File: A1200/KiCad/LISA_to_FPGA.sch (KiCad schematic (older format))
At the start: 27 parts, among them J1 Conn_01x04, J2 Conn_01x40, U1 LM1117-3.3, U2 74LVC162244ADGG, U3 74LVC162244ADGG, U4 LISA, U5 RP2354B

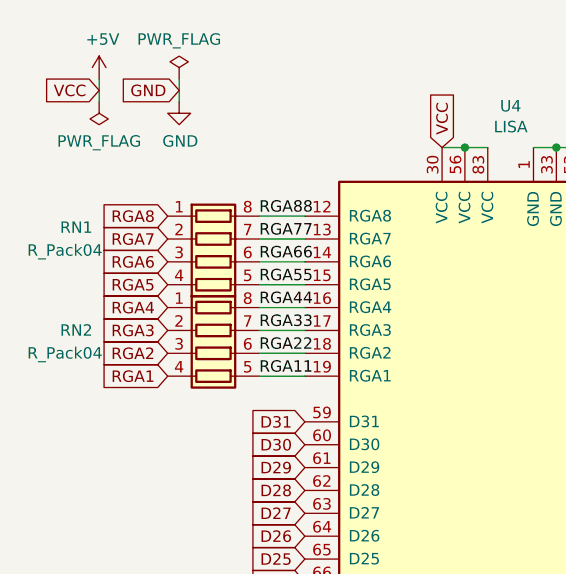
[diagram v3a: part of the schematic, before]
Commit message: Go to 4 layer and route RGA tracks
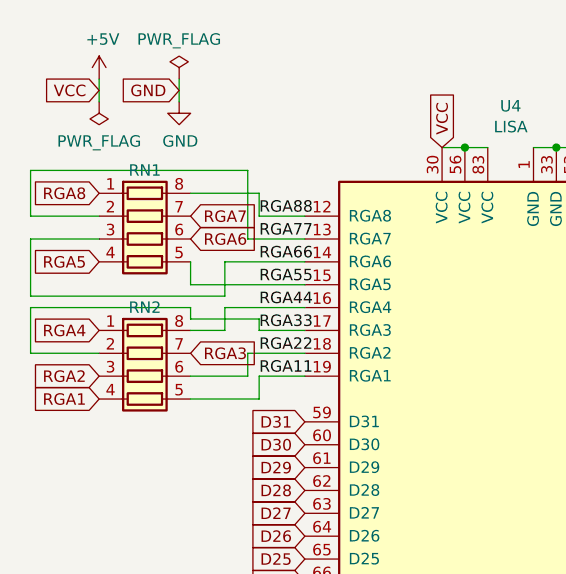
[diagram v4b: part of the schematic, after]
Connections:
- net RGA3: now also RN2.7 (R2.2); no longer RN2.2 (R2.1)
- net RGA33: now also RN2.2 (R2.1); no longer RN2.7 (R2.2)
- net RGA6: now also RN1.6 (R3.2); no longer RN1.3 (R3.1)
- net RGA66: now also RN1.3 (R3.1); no longer RN1.6 (R3.2)
- net RGA7: now also RN1.7 (R2.2); no longer RN1.2 (R2.1)
- net RGA77: now also RN1.2 (R2.1); no longer RN1.7 (R2.2)
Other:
- moved on the sheet: RN1, RN2
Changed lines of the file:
@@
 GND
 NoConn ~ 3500 1350
-Text GLabel 1100 2050 0    50   Input ~ 0
+Text GLabel 800  2150 0    50   Input ~ 0
 RGA1
-Text GLabel 1100 1950 0    50   Input ~ 0
+Text GLabel 800  2050 0    50   Input ~ 0
 RGA2
-Text GLabel 1100 1850 0    50   Input ~ 0
+Text GLabel 1200 1950 2    50   Input ~ 0
 RGA3
-Text GLabel 1100 1750 0    50   Input ~ 0
+Text GLabel 800  1850 0    50   Input ~ 0
 RGA4
-Text GLabel 1100 1650 0    50   Input ~ 0
+Text GLabel 800  1550 0    50   Input ~ 0
 RGA5
-Text GLabel 1100 1550 0    50   Input ~ 0
+Text GLabel 1200 1450 2    50   Input ~ 0
 RGA6
-Text GLabel 1100 1450 0    50   Input ~ 0
+Text GLabel 1200 1350 2    50   Input ~ 0
 RGA7
-Text GLabel 1100 1350 0    50   Input ~ 0
+Text GLabel 800  1250 0    50   Input ~ 0
 RGA8
 Text GLabel 1700 2250 0    50   Input ~ 0
@@
 L Device:R_Pack04 RN1
 U 1 1 6B113332
-P 1300 1550
-F 0 "RN1" V 1150 950 50  0000 C CNN
-F 1 "R_Pack04" V 1250 900 50  0000 C CNN
-F 2 "Resistor_SMD:R_Array_Convex_4x0603" V 1575 1550 50  0001 C CNN
-F 3 "~" H 1300 1550 50  0001 C CNN
-	1    1300 1550
+P 1000 1450
+F 0 "RN1" V 700 1450 50  0000 C CNN
+F 1 "R_Pack04" V 950 800 50  0001 C CNN
+F 2 "Resistor_SMD:R_Array_Convex_4x0603" V 1275 1450 50  0001 C CNN
+F 3 "~" H 1000 1450 50  0001 C CNN
+	1    1000 1450
 	0    1    1    0
 $EndComp
@@
 Wire Wire Line
 	1700 1350 1500 1350
-Wire Wire Line
-	1700 1450 1500 1450
-Wire Wire Line
-	1700 1550 1500 1550
-Wire Wire Line
-	1700 1650 1500 1650
 Text Label 1500 1350 0    50   ~ 0
 RGA88
@@
 L Device:R_Pack04 RN2
 U 1 1 6B1A8BE3
-P 1300 1950
-F 0 "RN2" V 1200 1350 50  0000 C CNN
-F 1 "R_Pack04" V 1300 1300 50  0000 C CNN
-F 2 "Resistor_SMD:R_Array_Convex_4x0603" V 1575 1950 50  0001 C CNN
-F 3 "~" H 1300 1950 50  0001 C CNN
-	1    1300 1950
+P 1000 2050
+F 0 "RN2" V 700 2050 50  0000 C CNN
+F 1 "R_Pack04" V 1000 1400 50  0001 C CNN
+F 2 "Resistor_SMD:R_Array_Convex_4x0603" V 1275 2050 50  0001 C CNN
+F 3 "~" H 1000 2050 50  0001 C CNN
+	1    1000 2050
 	0    1    1    0
 $EndComp
-Wire Wire Line
-	1500 1750 1700 1750
-Wire Wire Line
-	1500 1850 1700 1850
-Wire Wire Line
-	1500 1950 1700 1950
 Wire Wire Line
 	1500 2050 1700 2050
@@
 Wire Wire Line
 	9300 5500 9550 5500
+Wire Wire Line
+	1350 1550 1350 1700
+Wire Wire Line
+	1350 1700 500  1700
+Wire Wire Line
+	500  1700 500  1450
+Wire Wire Line
+	500  1450 800  1450
+Wire Wire Line
+	1350 1550 1700 1550
+Wire Wire Line
+	1200 1650 1200 1550
+Wire Wire Line
+	1200 1650 1700 1650
+Wire Wire Line
+	1700 1750 1350 1750
+Wire Wire Line
+	1350 1750 1350 1850
+Wire Wire Line
+	1350 1850 1200 1850
+Wire Wire Line
+	1200 1800 1200 1750
+Wire Wire Line
+	1200 1750 500  1750
+Wire Wire Line
+	1500 1800 1500 1850
+Wire Wire Line
+	1200 1800 1500 1800
+Wire Wire Line
+	1500 1850 1700 1850
+Wire Wire Line
+	1500 2050 1500 2150
+Wire Wire Line
+	1500 2150 1200 2150
+Wire Wire Line
+	1450 1450 1700 1450
+Wire Wire Line
+	1200 1250 1500 1250
+Wire Wire Line
+	1500 1250 1500 1350
+Wire Wire Line
+	1450 1450 1450 1150
+Wire Wire Line
+	1450 1150 500  1150
+Wire Wire Line
+	500  1150 500  1350
+Wire Wire Line
+	500  1350 800  1350
+Wire Wire Line
+	1700 1950 1450 1950
+Wire Wire Line
+	1450 1950 1450 2050
+Wire Wire Line
+	1450 2050 1200 2050
+Wire Wire Line
+	500  1750 500  1950
+Wire Wire Line
+	500  1950 800  1950
 $EndSCHEMATC

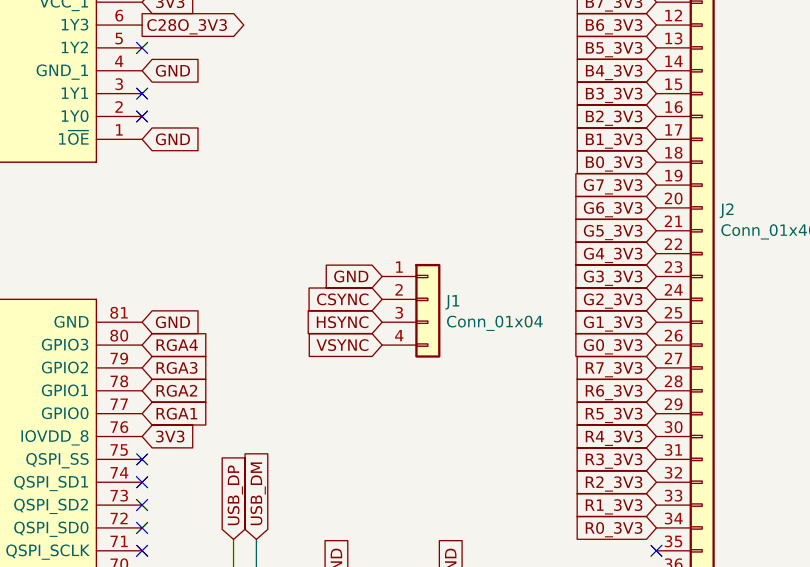
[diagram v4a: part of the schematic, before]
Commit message: Remove 4-pin header and replace with 1-pin header for Csync only
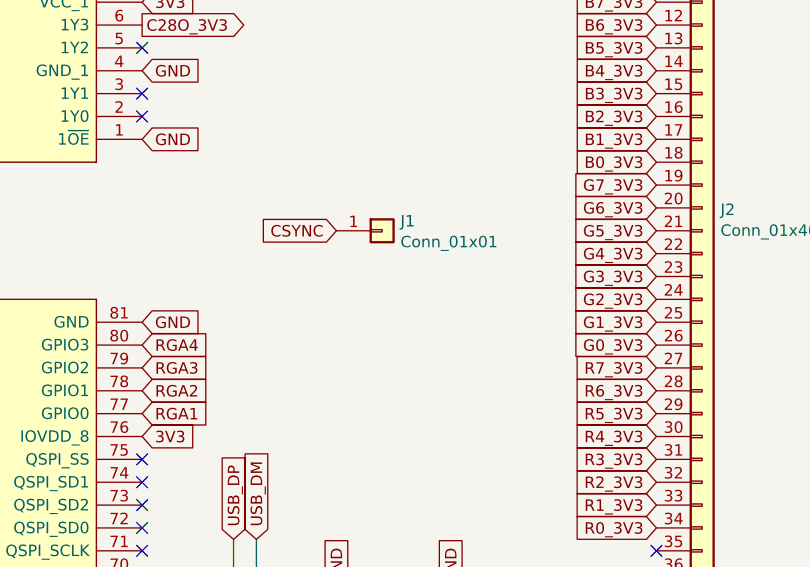
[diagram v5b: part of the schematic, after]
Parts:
- removed J1: Conn_01x04, Connector_PinHeader_2.54mm:PinHeader_1x04_P2.54mm_Horizontal, symbol Connector_Generic:Conn_01x04
- added J1: Conn_01x01, Connector_PinHeader_2.54mm:PinHeader_1x01_P2.54mm_Horizontal, symbol Connector_Generic:Conn_01x01
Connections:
- net CSYNC: now also J1.1 (Pin_1)
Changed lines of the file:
@@
 Text GLabel 3500 4850 2    50   Output ~ 0
 C28O
-$Comp
-L Connector_Generic:Conn_01x04 J1
-U 1 1 6690A0D6
-P 9450 3800
-F 0 "J1" H 9530 3792 50  0000 L CNN
-F 1 "Conn_01x04" H 9530 3701 50  0000 L CNN
-F 2 "Connector_PinHeader_2.54mm:PinHeader_1x04_P2.54mm_Horizontal" H 9450 3800 50  0001 C CNN
-F 3 "~" H 9450 3800 50  0001 C CNN
-	1    9450 3800
-	1    0    0    -1
-$EndComp
-Text GLabel 9250 3700 0    50   Input ~ 0
-GND
 NoConn ~ 8200 3000
 NoConn ~ 8200 2900
@@
 Text GLabel 6050 900  2    50   Output ~ 0
 R0_3V3
-Text GLabel 9250 4000 0    50   Input ~ 0
-VSYNC
-Text GLabel 9250 3900 0    50   Input ~ 0
-HSYNC
 Text GLabel 6050 1400 2    50   Input ~ 0
 3V3
@@
 Text GLabel 8200 2000 2    50   Output ~ 0
 B7_3V3
-Text GLabel 9250 3800 0    50   Input ~ 0
+Text GLabel 9050 3500 0    50   Input ~ 0
 CSYNC
 Text GLabel 8200 1800 2    50   Output ~ 0
@@
 Wire Wire Line
 	500  1950 800  1950
+$Comp
+L Connector_Generic:Conn_01x01 J1
+U 1 1 6ADA5BCA
+P 9250 3500
+F 0 "J1" H 9330 3542 50  0000 L CNN
+F 1 "Conn_01x01" H 9330 3451 50  0000 L CNN
+F 2 "Connector_PinHeader_2.54mm:PinHeader_1x01_P2.54mm_Horizontal" H 9250 3500 50  0001 C CNN
+F 3 "~" H 9250 3500 50  0001 C CNN
+	1    9250 3500
+	1    0    0    -1
+$EndComp
 $EndSCHEMATC

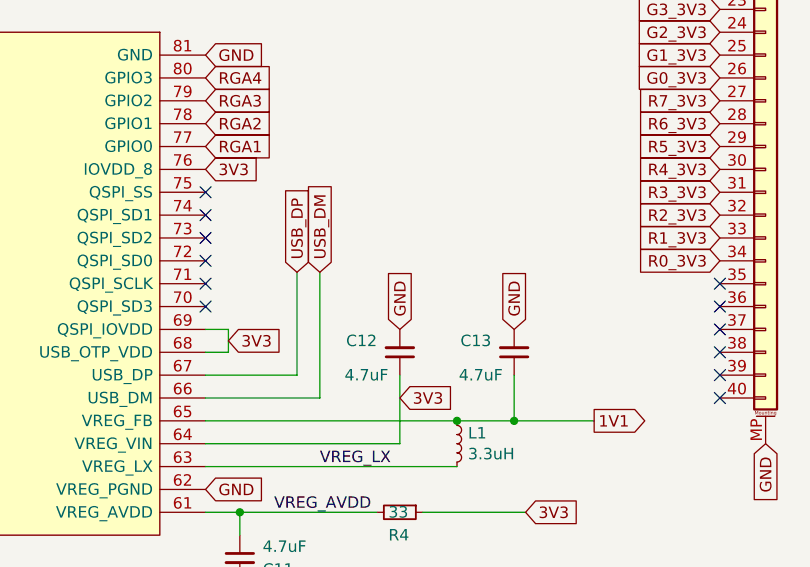
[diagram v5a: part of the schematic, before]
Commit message: Add 27 Ohm series resistor for the USB signals
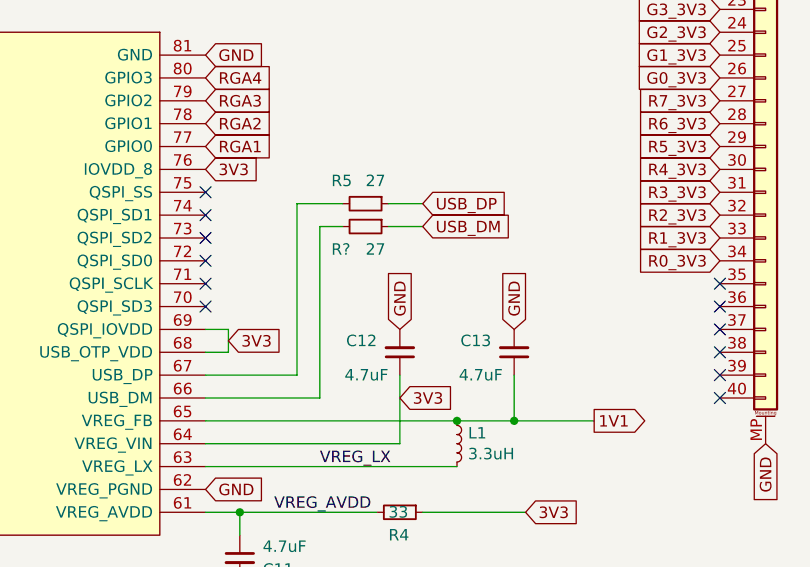
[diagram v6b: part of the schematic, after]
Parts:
- added R5, R?: 27, Resistor_SMD:R_0603_1608Metric_Pad0.98x0.95mm_HandSolder, symbol Device:R_Small
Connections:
- net USB_DM: now also R?.1; no longer U5.66 (USB_DM)
- net USB_DP: now also R5.1; no longer U5.67 (USB_DP)
- new net: R5.2, U5.67 (USB_DP)
- new net: R?.2, U5.66 (USB_DM)
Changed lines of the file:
@@
 Text GLabel 10450 2300 0    50   Output ~ 0
 RX
-Text GLabel 8600 4850 1    50   Input ~ 0
+Text GLabel 9150 4550 2    50   Input ~ 0
 USB_DP
-Text GLabel 8700 4850 1    50   Input ~ 0
+Text GLabel 9150 4650 2    50   Input ~ 0
 USB_DM
 Text GLabel 8300 5150 2    50   Input ~ 0
@@
 	8200 5600 9050 5600
 Wire Wire Line
-	8600 5300 8600 4850
-Wire Wire Line
-	8700 4850 8700 5400
-Wire Wire Line
 	8200 5300 8600 5300
 Wire Wire Line
@@
 	1    0    0    -1
 $EndComp
+$Comp
+L Device:R_Small R5
+U 1 1 6ADD5018
+P 8900 4550
+F 0 "R5" V 8800 4400 50  0000 L CNN
+F 1 "27" V 8800 4550 50  0000 L CNN
+F 2 "Resistor_SMD:R_0603_1608Metric_Pad0.98x0.95mm_HandSolder" H 8900 4550 50  0001 C CNN
+F 3 "~" H 8900 4550 50  0001 C CNN
+	1    8900 4550
+	0    1    1    0
+$EndComp
+Wire Wire Line
+	8600 4550 8600 5300
+Wire Wire Line
+	8600 4550 8800 4550
+$Comp
+L Device:R_Small R?
+U 1 1 6ADF2133
+P 8900 4650
+F 0 "R?" V 9000 4500 50  0000 L CNN
+F 1 "27" V 9000 4650 50  0000 L CNN
+F 2 "Resistor_SMD:R_0603_1608Metric_Pad0.98x0.95mm_HandSolder" H 8900 4650 50  0001 C CNN
+F 3 "~" H 8900 4650 50  0001 C CNN
+	1    8900 4650
+	0    1    1    0
+$EndComp
+Wire Wire Line
+	8700 4650 8800 4650
+Wire Wire Line
+	8700 4650 8700 5400
+Wire Wire Line
+	9000 4550 9150 4550
+Wire Wire Line
+	9000 4650 9150 4650
 $EndSCHEMATC

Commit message: Add 330 Ohm resistor pack RN3 and route D31-D28 to RP2354B
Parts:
- added RN3: R_Pack04, Resistor_SMD:R_Array_Convex_4x0603, symbol Device:R_Pack04
- gave numbers to parts that had none: 1
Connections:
- net D28: now also RN3.5 (R4.2); no longer U4.62 (D28)
- net D29: now also RN3.6 (R3.2); no longer U4.61 (D29)
- net D30: now also RN3.7 (R2.2); no longer U4.60 (D30)
- net D31: now also RN3.8 (R1.2); no longer U4.59 (D31)
- net RGA11 renamed RGA01
- net RGA22 renamed RGA02
- net RGA33 renamed RGA03
- net RGA44 renamed RGA04
- net RGA55 renamed RGA05
- net RGA66 renamed RGA06
- net RGA77 renamed RGA07
- net RGA88 renamed RGA08
- new net D028: RN3.4 (R4.1), U4.62 (D28)
- new net D029: RN3.3 (R3.1), U4.61 (D29)
- new net D030: RN3.2 (R2.1), U4.60 (D30)
- new net D031: RN3.1 (R1.1), U4.59 (D31)
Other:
- moved on the sheet: RN1, RN2
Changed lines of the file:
@@
 GND
 NoConn ~ 3500 1350
-Text GLabel 800  2150 0    50   Input ~ 0
+Text GLabel 750  2050 0    50   Output ~ 0
 RGA1
-Text GLabel 800  2050 0    50   Input ~ 0
+Text GLabel 750  1950 0    50   Output ~ 0
 RGA2
-Text GLabel 1200 1950 2    50   Input ~ 0
+Text GLabel 1150 1850 2    50   Output ~ 0
 RGA3
-Text GLabel 800  1850 0    50   Input ~ 0
+Text GLabel 750  1750 0    50   Output ~ 0
 RGA4
-Text GLabel 800  1550 0    50   Input ~ 0
+Text GLabel 750  1650 0    50   Output ~ 0
 RGA5
-Text GLabel 1200 1450 2    50   Input ~ 0
+Text GLabel 1150 1550 2    50   Output ~ 0
 RGA6
-Text GLabel 1200 1350 2    50   Input ~ 0
+Text GLabel 1150 1450 2    50   Output ~ 0
 RGA7
-Text GLabel 800  1250 0    50   Input ~ 0
+Text GLabel 750  1350 0    50   Output ~ 0
 RGA8
-Text GLabel 1700 2250 0    50   Input ~ 0
+Text GLabel 1150 2250 2    50   Output ~ 0
 D31
-Text GLabel 1700 2350 0    50   Input ~ 0
+Text GLabel 1150 2350 2    50   Output ~ 0
 D30
-Text GLabel 1700 2450 0    50   Input ~ 0
+Text GLabel 1150 2450 2    50   Output ~ 0
 D29
-Text GLabel 1700 2550 0    50   Input ~ 0
+Text GLabel 1150 2550 2    50   Output ~ 0
 D28
 Text GLabel 1700 2650 0    50   Input ~ 0
@@
 L Device:R_Pack04 RN1
 U 1 1 6B113332
-P 1000 1450
-F 0 "RN1" V 700 1450 50  0000 C CNN
-F 1 "R_Pack04" V 950 800 50  0001 C CNN
-F 2 "Resistor_SMD:R_Array_Convex_4x0603" V 1275 1450 50  0001 C CNN
-F 3 "~" H 1000 1450 50  0001 C CNN
-	1    1000 1450
+P 950 1550
+F 0 "RN1" V 900 1550 50  0000 C CNN
+F 1 "R_Pack04" V 900 900 50  0001 C CNN
+F 2 "Resistor_SMD:R_Array_Convex_4x0603" V 1225 1550 50  0001 C CNN
+F 3 "~" H 950 1550 50  0001 C CNN
+	1    950  1550
 	0    1    1    0
 $EndComp
@@
 Wire Wire Line
 	6650 2600 6650 2850
-Wire Wire Line
-	1700 1350 1500 1350
-Text Label 1500 1350 0    50   ~ 0
-RGA88
-Text Label 1500 1450 0    50   ~ 0
-RGA77
-Text Label 1500 1550 0    50   ~ 0
-RGA66
-Text Label 1500 1650 0    50   ~ 0
-RGA55
 $Comp
 L Device:R_Pack04 RN2
 U 1 1 6B1A8BE3
-P 1000 2050
-F 0 "RN2" V 700 2050 50  0000 C CNN
-F 1 "R_Pack04" V 1000 1400 50  0001 C CNN
-F 2 "Resistor_SMD:R_Array_Convex_4x0603" V 1275 2050 50  0001 C CNN
-F 3 "~" H 1000 2050 50  0001 C CNN
-	1    1000 2050
-	0    1    1    0
-$EndComp
-Wire Wire Line
-	1500 2050 1700 2050
-Text Label 1500 1750 0    50   ~ 0
-RGA44
-Text Label 1500 1850 0    50   ~ 0
-RGA33
-Text Label 1500 1950 0    50   ~ 0
-RGA22
-Text Label 1500 2050 0    50   ~ 0
-RGA11
+P 950 1950
+F 0 "RN2" V 900 1950 50  0000 C CNN
+F 1 "R_Pack04" V 950 1300 50  0001 C CNN
+F 2 "Resistor_SMD:R_Array_Convex_4x0603" V 1225 1950 50  0001 C CNN
+F 3 "~" H 950 1950 50  0001 C CNN
+	1    950  1950
+	0    1    1    0
+$EndComp
+Text Label 1450 1750 0    50   ~ 0
+RGA04
+Text Label 1450 1950 0    50   ~ 0
+RGA02
+Text Label 1450 2050 0    50   ~ 0
+RGA01
 Text GLabel 4500 5400 0    50   Output ~ 0
 TX
@@
 Wire Wire Line
 	9300 5500 9550 5500
-Wire Wire Line
-	1350 1550 1350 1700
-Wire Wire Line
-	1350 1700 500  1700
-Wire Wire Line
-	500  1700 500  1450
-Wire Wire Line
-	500  1450 800  1450
-Wire Wire Line
-	1350 1550 1700 1550
-Wire Wire Line
-	1200 1650 1200 1550
-Wire Wire Line
-	1200 1650 1700 1650
-Wire Wire Line
-	1700 1750 1350 1750
-Wire Wire Line
-	1350 1750 1350 1850
-Wire Wire Line
-	1350 1850 1200 1850
-Wire Wire Line
-	1200 1800 1200 1750
-Wire Wire Line
-	1200 1750 500  1750
-Wire Wire Line
-	1500 1800 1500 1850
-Wire Wire Line
-	1200 1800 1500 1800
-Wire Wire Line
-	1500 1850 1700 1850
-Wire Wire Line
-	1500 2050 1500 2150
-Wire Wire Line
-	1500 2150 1200 2150
-Wire Wire Line
-	1450 1450 1700 1450
-Wire Wire Line
-	1200 1250 1500 1250
-Wire Wire Line
-	1500 1250 1500 1350
-Wire Wire Line
-	1450 1450 1450 1150
-Wire Wire Line
-	1450 1150 500  1150
-Wire Wire Line
-	500  1150 500  1350
-Wire Wire Line
-	500  1350 800  1350
-Wire Wire Line
-	1700 1950 1450 1950
-Wire Wire Line
-	1450 1950 1450 2050
-Wire Wire Line
-	1450 2050 1200 2050
-Wire Wire Line
-	500  1750 500  1950
-Wire Wire Line
-	500  1950 800  1950
 $Comp
 L Connector_Generic:Conn_01x01 J1
@@
 	8600 4550 8800 4550
 $Comp
-L Device:R_Small R?
+L Device:R_Small R6
 U 1 1 6ADF2133
 P 8900 4650
-F 0 "R?" V 9000 4500 50  0000 L CNN
+F 0 "R6" V 9000 4500 50  0000 L CNN
 F 1 "27" V 9000 4650 50  0000 L CNN
 F 2 "Resistor_SMD:R_0603_1608Metric_Pad0.98x0.95mm_HandSolder" H 8900 4650 50  0001 C CNN
@@
 Wire Wire Line
 	9000 4650 9150 4650
+$Comp
+L Device:R_Pack04 RN3
+U 1 1 6AE1A3D3
+P 950 2450
+F 0 "RN3" V 900 2450 50  0000 C CNN
+F 1 "R_Pack04" V 950 1800 50  0001 C CNN
+F 2 "Resistor_SMD:R_Array_Convex_4x0603" V 1225 2450 50  0001 C CNN
+F 3 "~" H 950 2450 50  0001 C CNN
+	1    950  2450
+	0    1    1    0
+$EndComp
+Text GLabel 750  1450 0    50   Input ~ 0
+RGA07
+Text GLabel 1700 1450 0    50   Output ~ 0
+RGA07
+Text GLabel 750  1550 0    50   Input ~ 0
+RGA06
+Text GLabel 1700 1550 0    50   Output ~ 0
+RGA06
+Wire Wire Line
+	1700 1350 1150 1350
+Wire Wire Line
+	1700 1650 1150 1650
+Text Label 1450 1350 0    50   ~ 0
+RGA08
+Text Label 1450 1650 0    50   ~ 0
+RGA05
+Text GLabel 750  1850 0    50   Input ~ 0
+RGA03
+Text GLabel 1700 1850 0    50   Output ~ 0
+RGA03
+Wire Wire Line
+	1700 1750 1150 1750
+Wire Wire Line
+	1700 1950 1150 1950
+Wire Wire Line
+	1700 2050 1150 2050
+Text GLabel 1700 2250 0    50   Output ~ 0
+D031
+Text GLabel 1700 2350 0    50   Output ~ 0
+D030
+Text GLabel 1700 2450 0    50   Output ~ 0
+D029
+Text GLabel 1700 2550 0    50   Output ~ 0
+D028
+Text GLabel 750  2250 0    50   Input ~ 0
+D031
+Text GLabel 750  2350 0    50   Input ~ 0
+D030
+Text GLabel 750  2450 0    50   Input ~ 0
+D029
+Text GLabel 750  2550 0    50   Input ~ 0
+D028
 $EndSCHEMATC
